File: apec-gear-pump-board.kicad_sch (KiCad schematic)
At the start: 7 parts, among them J1 Screw_Terminal_01x06, J2 Screw_Terminal_01x02, J3 Screw_Terminal_01x04

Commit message: Fixed mistake
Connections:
- net at J3.4 (SPEED_IN), R1.1: no longer C1.1
- net at J1.3 (SPEED_IN), R1.2: now also C1.1
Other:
- moved on the sheet: C1
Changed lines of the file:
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@@
 (kicad_sch (version 20230121) (generator eeschema)
   (paper "A4")
-  (junction (at 54.61 45.72) (diameter 0) (color 0 0 0 0)
+  (junction (at 63.5 45.72) (diameter 0) (color 0 0 0 0)
   )
-  (junction (at 54.61 40.64) (diameter 0) (color 0 0 0 0)
+  (junction (at 63.5 40.64) (diameter 0) (color 0 0 0 0)
   )
-  (wire (pts (xy 46.99 45.72) (xy 54.61 45.72))
+  (wire (pts (xy 46.99 45.72) (xy 63.5 45.72))
+    (stroke (width 0) (type default))
+  )
+  (wire (pts (xy 63.5 40.64) (xy 68.58 40.64))
     (stroke (width 0) (type default))
   )
@@
     (stroke (width 0) (type default))
   )
-  (wire (pts (xy 54.61 40.64) (xy 49.53 40.64))
+  (wire (pts (xy 49.53 40.64) (xy 54.61 40.64))
+    (stroke (width 0) (type default))
+  )
+  (wire (pts (xy 63.5 45.72) (xy 81.28 45.72))
     (stroke (width 0) (type default))
   )
@@
     (stroke (width 0) (type default))
   )
-  (wire (pts (xy 68.58 40.64) (xy 66.04 40.64))
+  (wire (pts (xy 59.69 40.64) (xy 63.5 40.64))
     (stroke (width 0) (type default))
   )
@@
   )
   (wire (pts (xy 71.12 31.75) (xy 71.12 40.64))
-    (stroke (width 0) (type default))
-  )
-  (wire (pts (xy 54.61 45.72) (xy 81.28 45.72))
-    (stroke (width 0) (type default))
-  )
-  (wire (pts (xy 54.61 40.64) (xy 60.96 40.64))
     (stroke (width 0) (type default))
   )
@@
     )
   )
-  (symbol (lib_id "Device:R_Small") (at 63.5 40.64 90) (unit 1)
+  (symbol (lib_id "Device:R_Small") (at 57.15 40.64 90) (unit 1)
     (in_bom yes) (on_board yes) (dnp no) (fields_autoplaced)
-    (property "Reference" "R1" (at 63.5 35.56 90)
+    (property "Reference" "R1" (at 57.15 35.56 90)
       (effects (font (size 1.27 1.27)))
     )
-    (property "Value" "R_Small" (at 63.5 38.1 90)
+    (property "Value" "R_Small" (at 57.15 38.1 90)
       (effects (font (size 1.27 1.27)))
     )
-    (property "Footprint" "Resistor_THT:R_Axial_DIN0204_L3.6mm_D1.6mm_P5.08mm_Horizontal" (at 63.5 40.64 0)
+    (property "Footprint" "Resistor_THT:R_Axial_DIN0204_L3.6mm_D1.6mm_P5.08mm_Horizontal" (at 57.15 40.64 0)
       (effects (font (size 1.27 1.27)) hide)
     )
-    (property "Datasheet" "~" (at 63.5 40.64 0)
+    (property "Datasheet" "~" (at 57.15 40.64 0)
       (effects (font (size 1.27 1.27)) hide)
     )
@@
     )
   )
-  (symbol (lib_id "Device:C_Small") (at 54.61 43.18 0) (unit 1)
+  (symbol (lib_id "Device:C_Small") (at 63.5 43.18 0) (unit 1)
     (in_bom yes) (on_board yes) (dnp no) (fields_autoplaced)
-    (property "Reference" "C1" (at 57.15 41.9163 0)
+    (property "Reference" "C1" (at 66.04 41.9163 0)
       (effects (font (size 1.27 1.27)) (justify left))
     )
-    (property "Value" "C_Small" (at 57.15 44.4563 0)
+    (property "Value" "C_Small" (at 66.04 44.4563 0)
       (effects (font (size 1.27 1.27)) (justify left))
     )
-    (property "Footprint" "Capacitor_THT:C_Rect_L4.6mm_W3.0mm_P2.50mm_MKS02_FKP02" (at 54.61 43.18 0)
+    (property "Footprint" "Capacitor_THT:C_Rect_L4.6mm_W3.0mm_P2.50mm_MKS02_FKP02" (at 63.5 43.18 0)
       (effects (font (size 1.27 1.27)) hide)
     )
-    (property "Datasheet" "~" (at 54.61 43.18 0)
+    (property "Datasheet" "~" (at 63.5 43.18 0)
       (effects (font (size 1.27 1.27)) hide)
     )

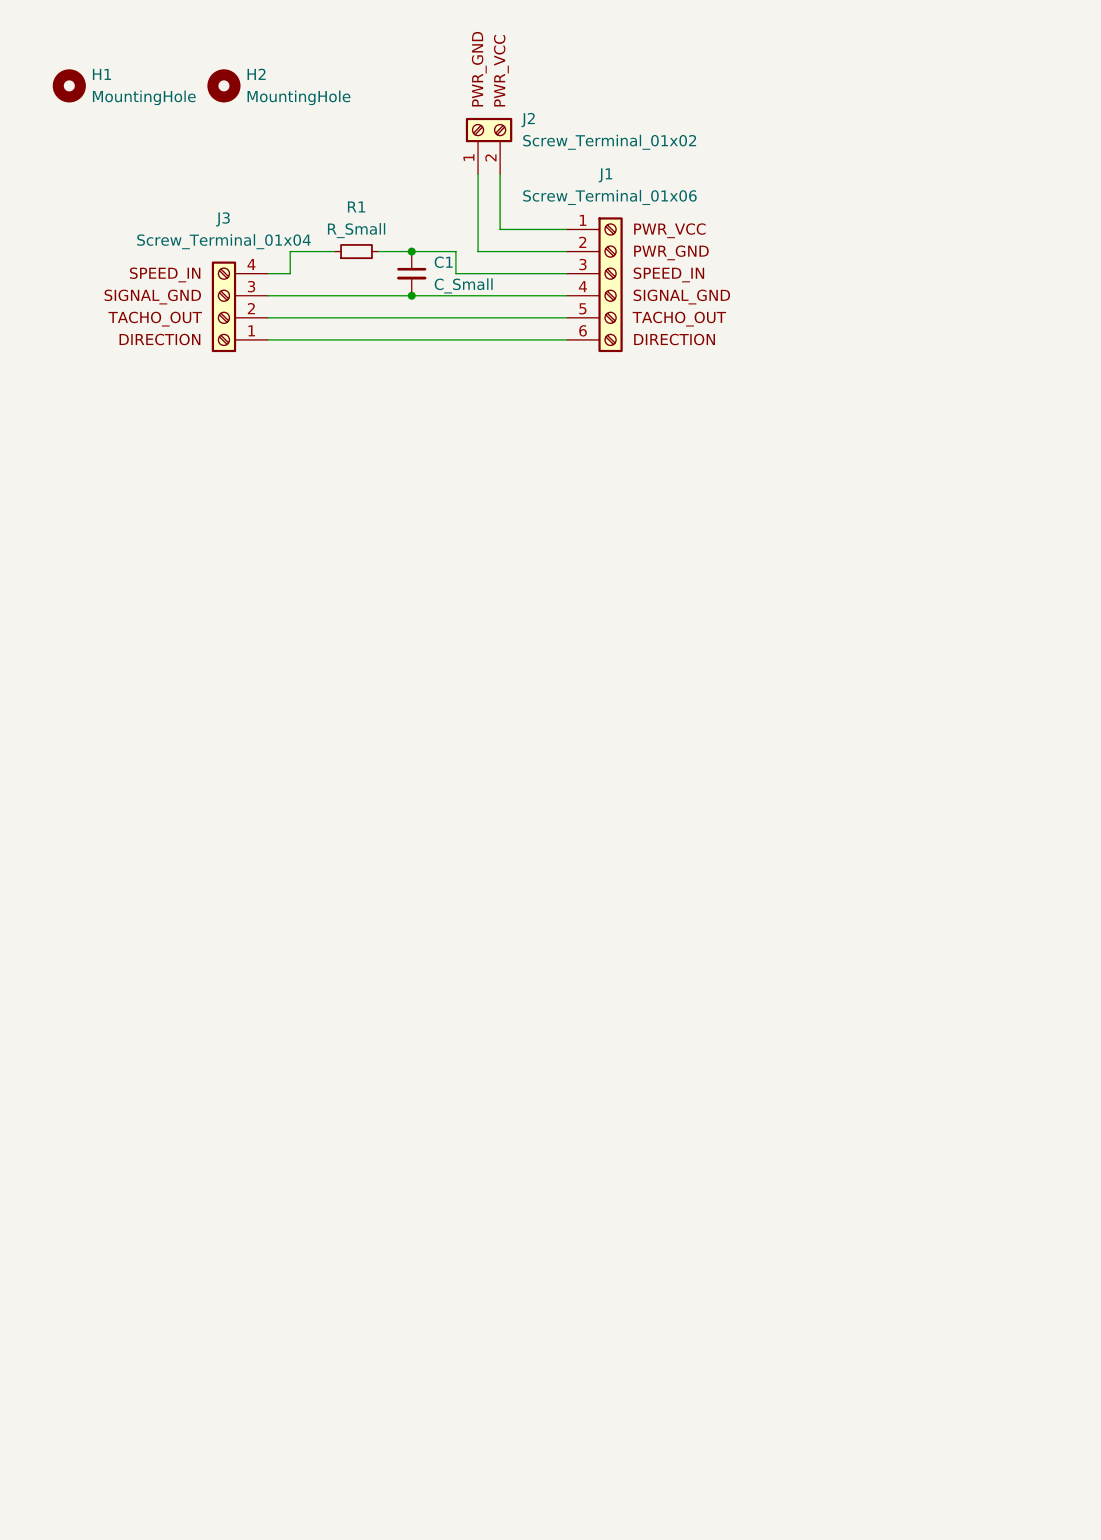
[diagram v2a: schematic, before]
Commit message: Updated the board to do level shifting
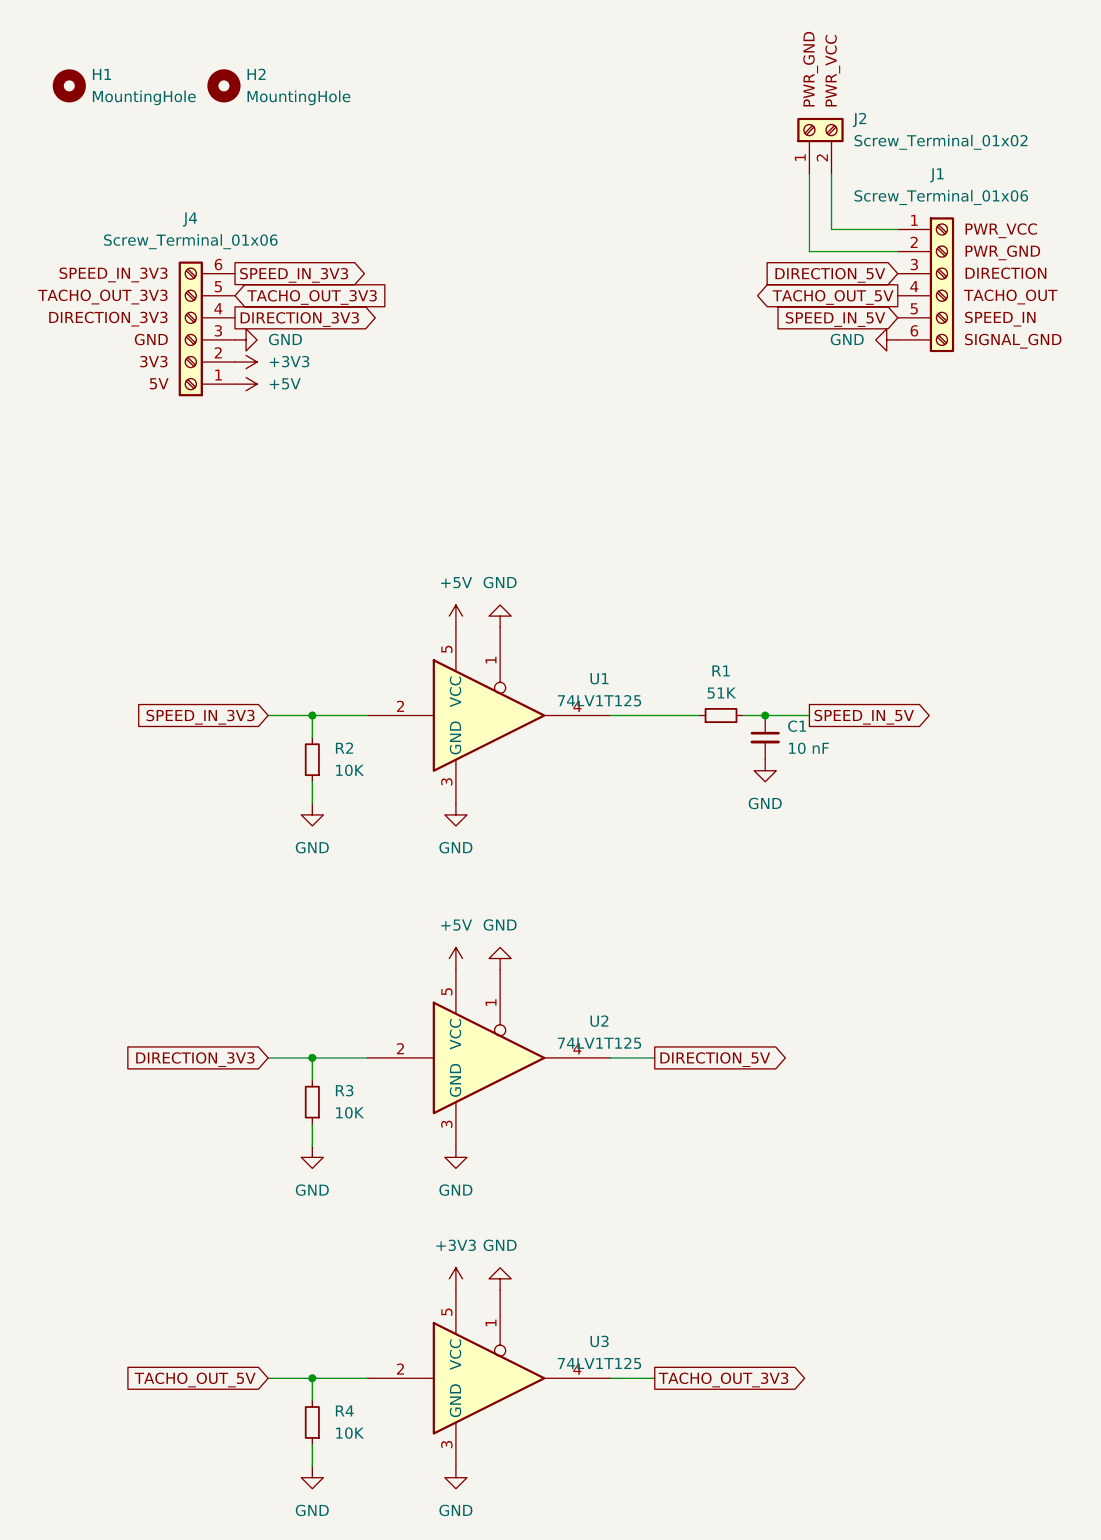
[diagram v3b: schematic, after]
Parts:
- removed J3: Screw_Terminal_01x04, Connector_PinHeader_2.54mm:PinHeader_1x04_P2.54mm_Vertical, symbol Connector:Screw_Terminal_01x04
- added J4: Screw_Terminal_01x06, Connector_PinHeader_2.54mm:PinHeader_1x06_P2.54mm_Vertical, symbol Connector:Screw_Terminal_01x06
- added R2, R3, R4: 10K, Resistor_SMD:R_1206_3216Metric_Pad1.30x1.75mm_HandSolder, symbol Device:R_Small
- added U1, U2, U3: 74LV1T125, Package_TO_SOT_SMD:SOT-23-5_HandSoldering, symbol 74xGxx:74LVC1G125
- C1: value C_Small -> 10 nF; footprint Capacitor_THT:C_Rect_L4.6mm_W3.0mm_P2.50mm_MKS02_FKP02 -> Capacitor_SMD:C_1206_3216Metric_Pad1.33x1.80mm_HandSolder; Digikey (none) -> 732-12286; LCSC (none) -> C1846
- R1: value R_Small -> 51K; footprint Resistor_THT:R_Axial_DIN0204_L3.6mm_D1.6mm_P5.08mm_Horizontal -> Resistor_SMD:R_1206_3216Metric_Pad1.30x1.75mm_HandSolder; Digikey (none) -> 311-51.0KFR; LCSC (none) -> C17992
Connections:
- net GND: now reaches J1.6 (DIRECTION)
- net GND: now also C1.2, J4.3 (Pin_3), R2.1, R3.1, R4.1, U1.1, U1.3 (GND), U2.1, U2.3 (GND), U3.1, U3.3 (GND)
- net SPEED_IN_5V: now reaches J1.5 (TACHO_OUT)
- net SPEED_IN_5V: now also C1.1, R1.2
- net TACHO_OUT_5V: now reaches J1.4 (SIGNAL_GND)
- net TACHO_OUT_5V: now also R4.2, U3.2; no longer C1.2
- net at R1.1: now also U1.4
- new net +3V3: J4.2 (Pin_2), U3.5 (VCC)
- new net +5V: J4.1 (Pin_1), U1.5 (VCC), U2.5 (VCC)
- new net DIRECTION_3V3: J4.4 (Pin_4), R3.2, U2.2
- new net DIRECTION_5V: J1.3 (SPEED_IN), U2.4
- new net SPEED_IN_3V3: J4.6 (Pin_6), R2.2, U1.2
- new net TACHO_OUT_3V3: J4.5 (Pin_5), U3.4
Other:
- moved on the sheet: J1, J2

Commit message: Added decoupling caps and Variegated Coffee logo
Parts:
- added C2, C3: 1 uF, Capacitor_SMD:C_1206_3216Metric_Pad1.33x1.80mm_HandSolder, symbol Device:C_Small
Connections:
- net +3V3: now also C3.1
- net +5V: now also C2.1
- net GND: now also C2.2, C3.2
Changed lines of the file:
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@@
+    )
+  )
+  (symbol (lib_id "power:+5V") (at 76.2 49.53 90) (unit 1)
+    (in_bom yes) (on_board yes) (dnp no) (fields_autoplaced)
+    (property "Reference" "#PWR019" (at 80.01 49.53 0)
+      (effects (font (size 1.27 1.27)) hide)
+    )
+    (property "Value" "+5V" (at 72.39 49.53 90)
+      (effects (font (size 1.27 1.27)) (justify left))
+    )
+    (property "Footprint" "" (at 76.2 49.53 0)
+      (effects (font (size 1.27 1.27)) hide)
+    )
+    (property "Datasheet" "" (at 76.2 49.53 0)
+      (effects (font (size 1.27 1.27)) hide)
+    )
+    (pin "1")
+    (instances
+      (project "apec-gear-pump-board"
+        (path "/f01ed30c-0f0a-4868-bb0f-e4c4d93b4399"
+          (reference "#PWR019") (unit 1)
+        )
+      )
     )
   )
@@
         (path "/f01ed30c-0f0a-4868-bb0f-e4c4d93b4399"
           (reference "#PWR015") (unit 1)
+        )
+      )
+    )
+  )
+  (symbol (lib_id "power:GND") (at 81.28 49.53 90) (unit 1)
+    (in_bom yes) (on_board yes) (dnp no) (fields_autoplaced)
+    (property "Reference" "#PWR020" (at 87.63 49.53 0)
+      (effects (font (size 1.27 1.27)) hide)
+    )
+    (property "Value" "GND" (at 85.09 49.53 90)
+      (effects (font (size 1.27 1.27)) (justify right))
+    )
+    (property "Footprint" "" (at 81.28 49.53 0)
+      (effects (font (size 1.27 1.27)) hide)
+    )
+    (property "Datasheet" "" (at 81.28 49.53 0)
+      (effects (font (size 1.27 1.27)) hide)
+    )
+    (pin "1")
+    (instances
+      (project "apec-gear-pump-board"
+        (path "/f01ed30c-0f0a-4868-bb0f-e4c4d93b4399"
+          (reference "#PWR020") (unit 1)
         )
       )
@@
     )
   )
+  (symbol (lib_id "power:GND") (at 81.28 59.69 90) (unit 1)
+    (in_bom yes) (on_board yes) (dnp no) (fields_autoplaced)
+    (property "Reference" "#PWR021" (at 87.63 59.69 0)
+      (effects (font (size 1.27 1.27)) hide)
+    )
+    (property "Value" "GND" (at 85.09 59.69 90)
+      (effects (font (size 1.27 1.27)) (justify right))
+    )
+    (property "Footprint" "" (at 81.28 59.69 0)
+      (effects (font (size 1.27 1.27)) hide)
+    )
+    (property "Datasheet" "" (at 81.28 59.69 0)
+      (effects (font (size 1.27 1.27)) hide)
+    )
+    (pin "1")
+    (instances
+      (project "apec-gear-pump-board"
+        (path "/f01ed30c-0f0a-4868-bb0f-e4c4d93b4399"
+          (reference "#PWR021") (unit 1)
+        )
+      )
+    )
+  )
   (symbol (lib_id "power:GND") (at 73.66 160.02 180) (unit 1)
     (in_bom yes) (on_board yes) (dnp no) (fields_autoplaced)
@@
         (path "/f01ed30c-0f0a-4868-bb0f-e4c4d93b4399"
           (reference "#PWR014") (unit 1)
+        )
+      )
+    )
+  )
+  (symbol (lib_id "Device:C_Small") (at 78.74 59.69 90) (unit 1)
+    (in_bom yes) (on_board yes) (dnp no) (fields_autoplaced)
+    (property "Reference" "C3" (at 78.7463 53.34 90)
+      (effects (font (size 1.27 1.27)))
+    )
+    (property "Value" "1 uF" (at 78.7463 55.88 90)
+      (effects (font (size 1.27 1.27)))
+    )
+    (property "Footprint" "Capacitor_SMD:C_1206_3216Metric_Pad1.33x1.80mm_HandSolder" (at 78.74 59.69 0)
+      (effects (font (size 1.27 1.27)) hide)
+    )
+    (property "Datasheet" "~" (at 78.74 59.69 0)
+      (effects (font (size 1.27 1.27)) hide)
+    )
+    (property "Digikey" "1276-1068" (at 78.74 59.69 0)
+      (effects (font (size 1.27 1.27)) hide)
+    )
+    (property "LCSC" "C1848" (at 78.74 59.69 0)
+      (effects (font (size 1.27 1.27)) hide)
+    )
+    (pin "1")
+    (pin "2")
+    (instances
+      (project "apec-gear-pump-board"
+        (path "/f01ed30c-0f0a-4868-bb0f-e4c4d93b4399"
+          (reference "C3") (unit 1)
         )
       )
@@
     )
   )
+  (symbol (lib_id "power:+3V3") (at 76.2 59.69 90) (unit 1)
+    (in_bom yes) (on_board yes) (dnp no) (fields_autoplaced)
+    (property "Reference" "#PWR018" (at 80.01 59.69 0)
+      (effects (font (size 1.27 1.27)) hide)
+    )
+    (property "Value" "+3V3" (at 72.39 59.69 90)
+      (effects (font (size 1.27 1.27)) (justify left))
+    )
+    (property "Footprint" "" (at 76.2 59.69 0)
+      (effects (font (size 1.27 1.27)) hide)
+    )
+    (property "Datasheet" "" (at 76.2 59.69 0)
+      (effects (font (size 1.27 1.27)) hide)
+    )
+    (pin "1")
+    (instances
+      (project "apec-gear-pump-board"
+        (path "/f01ed30c-0f0a-4868-bb0f-e4c4d93b4399"
+          (reference "#PWR018") (unit 1)
+        )
+      )
+    )
+  )
   (symbol (lib_id "74xGxx:74LVC1G125") (at 73.66 170.18 0) (unit 1)
     (in_bom yes) (on_board yes) (dnp no) (fields_autoplaced)
@@
         )
       )
+    )
+  )
+  (symbol (lib_id "Device:C_Small") (at 78.74 49.53 90) (unit 1)
+    (in_bom yes) (on_board yes) (dnp no) (fields_autoplaced)
+    (property "Reference" "C2" (at 78.7463 43.18 90)
+      (effects (font (size 1.27 1.27)))
+    )
+    (property "Value" "1 uF" (at 78.7463 45.72 90)
+      (effects (font (size 1.27 1.27)))
+    )
+    (property "Footprint" "Capacitor_SMD:C_1206_3216Metric_Pad1.33x1.80mm_HandSolder" (at 78.74 49.53 0)
+      (effects (font (size 1.27 1.27)) hide)
+    )
+    (property "Datasheet" "~" (at 78.74 49.53 0)
+      (effects (font (size 1.27 1.27)) hide)
+    )
+    (property "Digikey" "1276-1068" (at 78.74 49.53 0)
+      (effects (font (size 1.27 1.27)) hide)
+    )
+    (property "LCSC" "C1848" (at 78.74 49.53 0)
+      (effects (font (size 1.27 1.27)) hide)
+    )
+    (pin "1")
+    (pin "2")
+    (instances
+      (project "apec-gear-pump-board"
+        (path "/f01ed30c-0f0a-4868-bb0f-e4c4d93b4399"
+          (reference "C2") (unit 1)
+        )
+      )
